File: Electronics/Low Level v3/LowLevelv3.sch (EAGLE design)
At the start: 53 parts, among them IC2 MCP4802, K1 ORWH-SH-105D1F,000, K3 ORWH-SH-105D1F,000, Q1 16MHz, T1 2N3904, T2 2N3904, U1 284512-4, U4 MCP2515, U5 MCP2551DIL08, X1 DB9 Plug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

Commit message: electronics update!
moved a lot of stuff to get the board smaller, added ground planes, added CANbus 3-pin header, fixed all the silkscreening
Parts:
- removed C12: 0.1uF, SparkFun-Capacitors:0.1UF-25V(+80/-20%)(0603)
- removed C14, C15: 22pF, SparkFun-Capacitors:22PF-PTH-2.54MM-200V-5%
- removed ODO_PORT_SELECT: (no value), pinhead:PINHD-1X3
- removed R12, R13: 100, SparkFun-Resistors:100OHM-1/10W-1%(0603)
- removed R14: 4.7K, SparkFun-Resistors:4.7KOHM-1/10W-1%(0603)
- removed U$2: CUI_JACKTHROUGH_HOLE, Elcano:CUI_JACKTHROUGH_HOLE
- added C13, C7: 560pF, rcl:C-US025-025X050
- added J1: (no value), SparkFun-Connectors:CONN_03-SCREW-5MM
- added R10, R7: 100, rcl:R-US_0207/10
- added R11: 4.7K, rcl:R-US_0207/10
- C1: value 560pF -> 0.1uF; device SparkFun-Capacitors:560PF-50V-5%(0603) -> rcl:C-US025-025X050; SPICEPREFIX C -> (none)
- C10: value 1 uF -> 0.1uF; device rcl:C-US025-030X050 -> rcl:C-US025-025X050
- C11: value 560pF -> 22pF; device SparkFun-Capacitors:560PF-50V-5%(0603) -> rcl:C-US025-025X050; SPICEPREFIX C -> (none)
- C6: value 0.1uF -> 22pF; device SparkFun-Capacitors:0.1UF-25V(+80/-20%)(0603) -> rcl:C-US025-025X050; SPICEPREFIX C -> (none)
- renumbered X1 to CANBUS
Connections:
- net SOLENOID_GND renamed SOLENOID_COMMON
- removed net N$1: C10.1, ODO_PORT_SELECT.3, U$2.P$1
- removed net N$15: D2.C, K3.C1
- removed net N$4: C4.1, ODO_PORT_SELECT.1, X4.1
- removed net N$8: D3.C, K1.C1
- new net RX3: CANBUS.8, COMM_DIG.7
- new net TX3: CANBUS.6, COMM_DIG.8
- net 5V: now also C1.1, C10.1, D2.C, D3.C, K1.C1, K3.C1; no longer C12.2, C6.2
- net CANH: now also J1.2, R7.2; no longer R13.2
- net CANL: now also J1.3, R10.2; no longer R12.2
- net GND: now also C1.2, C11.2, C13.2, C6.2, C7.2, CANBUS.1, J1.1, R11.2; no longer C1.1, C11.1, C12.1, C14.1, C15.1, C6.1, R14.1, U$2.P$2, U$2.P$3
- net N$10: now also C13.1, R7.1; no longer C11.2, R13.1
- net N$14: now also R11.1; no longer R14.2
- net N$17: now also C6.1; no longer C15.2
- net N$18: now also C11.1; no longer C14.2
- net N$9: now also C7.1, R10.1; no longer C1.2, R12.1
- net WHEELROTATION: now also C4.1, X4.1; no longer ODO_PORT_SELECT.2
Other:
- moved on the sheet: C1, C10, C11, C6, D1, U1

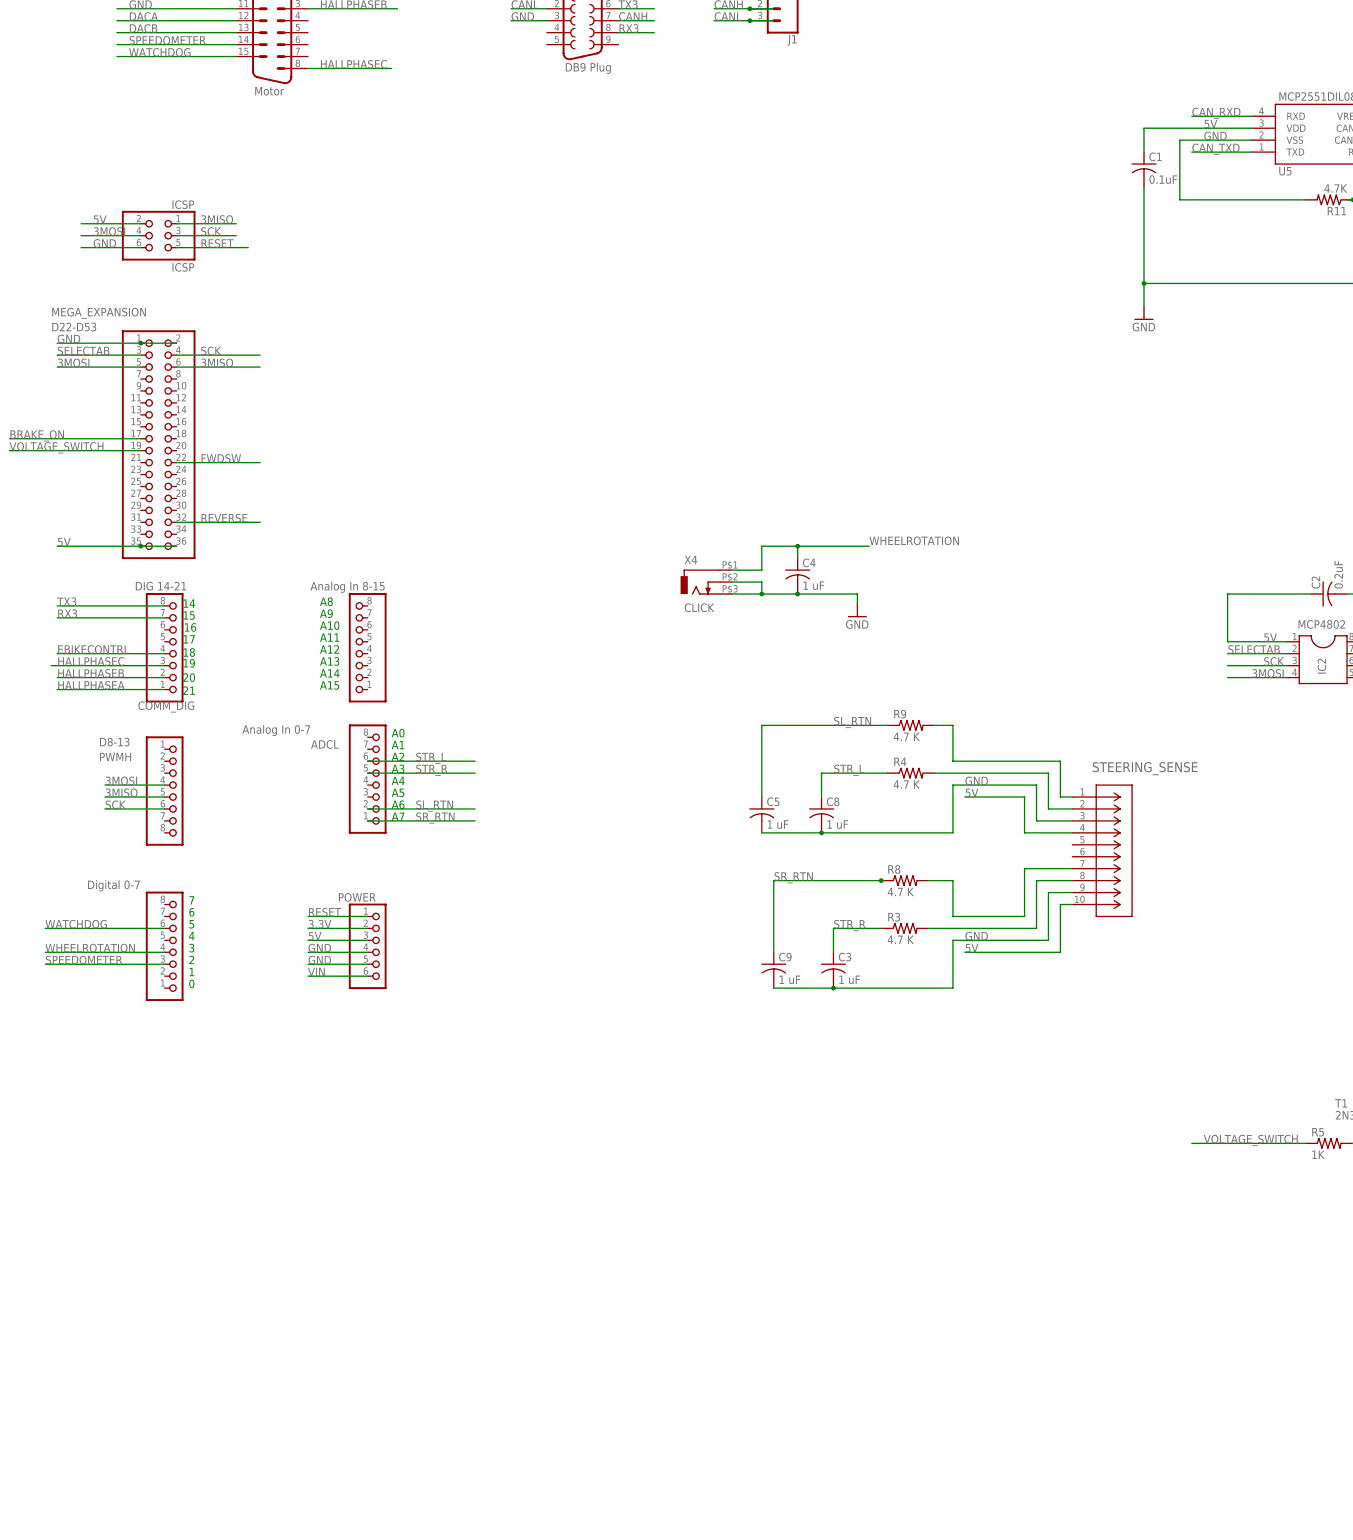
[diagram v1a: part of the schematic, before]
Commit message: added PWM output on steering header and 120ohm terminating resistor for CAN
forgot to commit this...
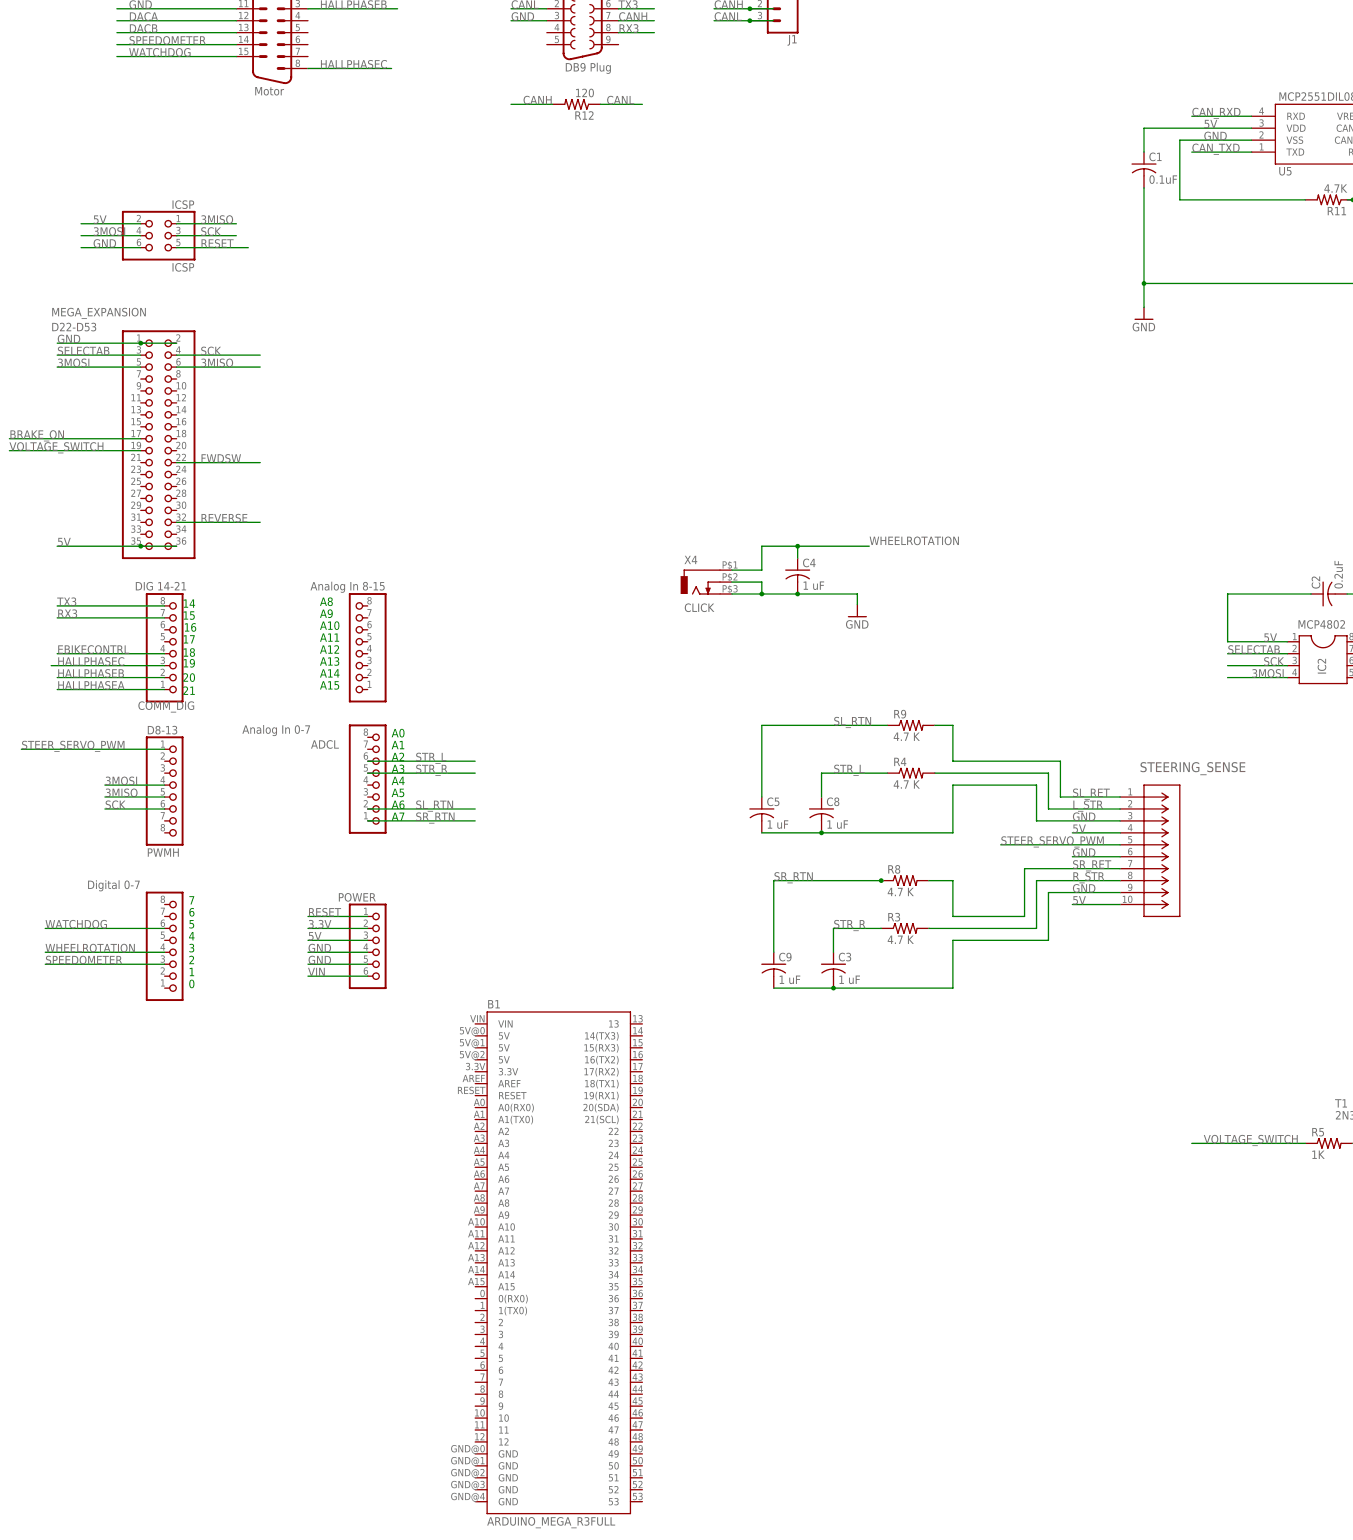
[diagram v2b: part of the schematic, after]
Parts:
- added B1: ARDUINO_MEGA_R3FULL, SparkFun-Boards:ARDUINO_MEGA_R3FULL
- added R12: 120, rcl:R-US_0207/10
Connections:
- new net STEER_SERVO_PWM: D8-13.1, STEERING_SENSE.5
- net CANH: now also R12.2
- net CANL: now also R12.1
- net GND: now also STEERING_SENSE.6
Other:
- moved on the sheet: STEERING_SENSE
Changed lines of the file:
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@@
 <part name="C11" library="rcl" library_urn="urn:adsk.eagle:library:334" deviceset="C-US" device="025-025X050" package3d_urn="urn:adsk.eagle:package:23629/2" value="22pF"/>
 <part name="J1" library="SparkFun-Connectors" library_urn="urn:adsk.eagle:library:513" deviceset="CONN_03" device="-SCREW-5MM" package3d_urn="urn:adsk.eagle:package:38070/1"/>
+<part name="R12" library="rcl" library_urn="urn:adsk.eagle:library:334" deviceset="R-US_" device="0207/10" package3d_urn="urn:adsk.eagle:package:23491/2" value="120"/>
+<part name="B1" library="SparkFun-Boards" library_urn="urn:adsk.eagle:library:509" deviceset="ARDUINO_MEGA_R3" device="FULL" package3d_urn="urn:adsk.eagle:package:37320/1"/>
 </parts>
 <sheets>
@@
 </instance>
 <instance part="D8-13" gate="A" x="58.42" y="55.88" smashed="yes">
-<attribute name="NAME" x="41.91" y="66.675" size="1.778" layer="95"/>
-<attribute name="VALUE" x="41.91" y="63.5" size="1.778" layer="96"/>
+<attribute name="NAME" x="52.07" y="69.215" size="1.778" layer="95"/>
+<attribute name="VALUE" x="52.07" y="43.18" size="1.778" layer="96"/>
 </instance>
 <instance part="GND5" gate="1" x="203.2" y="94.234" smashed="yes">
@@
 <attribute name="VALUE" x="383.52096875" y="-27.711740625" size="1.77906875" layer="96"/>
 </instance>
-<instance part="STEERING_SENSE" gate="A" x="248.92" y="55.88" smashed="yes">
-<attribute name="NAME" x="253.0856" y="61.1886" size="2.0828" layer="95" ratio="6" rot="SR0"/>
+<instance part="STEERING_SENSE" gate="A" x="259.08" y="55.88" smashed="yes">
+<attribute name="NAME" x="263.2456" y="61.1886" size="2.0828" layer="95" ratio="6" rot="SR0"/>
 </instance>
 <instance part="C7" gate="G$1" x="327.66" y="175.26" smashed="yes">
@@
 <attribute name="VALUE" x="190.5" y="230.886" size="1.778" layer="96" font="vector" rot="R180"/>
 <attribute name="NAME" x="190.5" y="217.932" size="1.778" layer="95" font="vector" rot="R180"/>
+</instance>
+<instance part="R12" gate="G$1" x="143.51" y="203.2" smashed="yes" rot="R180">
+<attribute name="NAME" x="147.32" y="201.7014" size="1.778" layer="95" rot="R180"/>
+<attribute name="VALUE" x="147.32" y="206.502" size="1.778" layer="96" rot="R180"/>
+</instance>
+<instance part="B1" gate="G$1" x="139.7" y="-43.18" smashed="yes">
+<attribute name="NAME" x="124.46" y="10.922" size="1.778" layer="95"/>
+<attribute name="VALUE" x="124.46" y="-99.06" size="1.778" layer="96"/>
 </instance>
 </instances>
@@
 </segment>
 <segment>
-<label x="226.06" y="22.86" size="1.778" layer="95"/>
-<wire x1="226.06" y1="22.86" x2="246.38" y2="22.86" width="0.1524" layer="91"/>
-<wire x1="246.38" y1="22.86" x2="246.38" y2="33.02" width="0.1524" layer="91"/>
+<label x="248.92" y="33.02" size="1.778" layer="95"/>
 <pinref part="STEERING_SENSE" gate="A" pin="10"/>
-<wire x1="246.38" y1="33.02" x2="248.92" y2="33.02" width="0.1524" layer="91"/>
+<wire x1="248.92" y1="33.02" x2="259.08" y2="33.02" width="0.1524" layer="91"/>
 </segment>
 <segment>
@@
 </segment>
 <segment>
-<wire x1="238.76" y1="55.88" x2="226.06" y2="55.88" width="0.1524" layer="91"/>
-<label x="226.06" y="55.88" size="1.778" layer="95"/>
-<wire x1="238.76" y1="55.88" x2="238.76" y2="48.26" width="0.1524" layer="91"/>
+<label x="248.92" y="48.26" size="1.778" layer="95"/>
 <pinref part="STEERING_SENSE" gate="A" pin="4"/>
-<wire x1="238.76" y1="48.26" x2="248.92" y2="48.26" width="0.1524" layer="91"/>
+<wire x1="248.92" y1="48.26" x2="259.08" y2="48.26" width="0.1524" layer="91"/>
 </segment>
 <segment>
@@
 <wire x1="223.52" y1="15.24" x2="223.52" y2="25.4" width="0.1524" layer="91"/>
 <wire x1="243.84" y1="25.4" x2="223.52" y2="25.4" width="0.1524" layer="91"/>
-<label x="226.06" y="25.4" size="1.778" layer="95"/>
+<label x="248.92" y="35.56" size="1.778" layer="95"/>
 <wire x1="243.84" y1="25.4" x2="243.84" y2="35.56" width="0.1524" layer="91"/>
 <pinref part="STEERING_SENSE" gate="A" pin="9"/>
-<wire x1="243.84" y1="35.56" x2="248.92" y2="35.56" width="0.1524" layer="91"/>
+<wire x1="243.84" y1="35.56" x2="259.08" y2="35.56" width="0.1524" layer="91"/>
 </segment>
 <segment>
@@
 <wire x1="195.58" y1="48.26" x2="223.52" y2="48.26" width="0.1524" layer="91"/>
 <wire x1="223.52" y1="48.26" x2="223.52" y2="58.42" width="0.1524" layer="91"/>
-<label x="226.06" y="58.42" size="1.778" layer="95"/>
+<label x="248.92" y="50.8" size="1.778" layer="95"/>
 <wire x1="195.58" y1="48.26" x2="182.88" y2="48.26" width="0.1524" layer="91"/>
 <junction x="195.58" y="48.26"/>
 <pinref part="STEERING_SENSE" gate="A" pin="3"/>
 <wire x1="241.3" y1="58.42" x2="241.3" y2="50.8" width="0.1524" layer="91"/>
-<wire x1="241.3" y1="50.8" x2="248.92" y2="50.8" width="0.1524" layer="91"/>
+<wire x1="241.3" y1="50.8" x2="259.08" y2="50.8" width="0.1524" layer="91"/>
 </segment>
 <segment>
@@
 <wire x1="137.16" y1="226.06" x2="129.54" y2="226.06" width="0.1524" layer="91"/>
 <label x="129.54" y="226.06" size="1.778" layer="95"/>
+</segment>
+<segment>
+<pinref part="STEERING_SENSE" gate="A" pin="6"/>
+<wire x1="259.08" y1="43.18" x2="248.92" y2="43.18" width="0.1524" layer="91"/>
+<label x="248.92" y="43.18" size="1.778" layer="95"/>
 </segment>
 </net>
@@
 <wire x1="241.3" y1="27.94" x2="241.3" y2="38.1" width="0.1524" layer="91"/>
 <pinref part="STEERING_SENSE" gate="A" pin="8"/>
-<wire x1="241.3" y1="38.1" x2="248.92" y2="38.1" width="0.1524" layer="91"/>
+<wire x1="241.3" y1="38.1" x2="259.08" y2="38.1" width="0.1524" layer="91"/>
+<label x="248.92" y="38.1" size="1.778" layer="95"/>
 </segment>
 </net>
@@
 <wire x1="243.84" y1="60.96" x2="243.84" y2="53.34" width="0.1524" layer="91"/>
 <pinref part="STEERING_SENSE" gate="A" pin="2"/>
-<wire x1="243.84" y1="53.34" x2="248.92" y2="53.34" width="0.1524" layer="91"/>
+<wire x1="243.84" y1="53.34" x2="259.08" y2="53.34" width="0.1524" layer="91"/>
+<label x="248.92" y="53.34" size="1.778" layer="95"/>
 </segment>
 </net>
@@
 <wire x1="246.38" y1="63.5" x2="246.38" y2="55.88" width="0.1524" layer="91"/>
 <pinref part="STEERING_SENSE" gate="A" pin="1"/>
-<wire x1="246.38" y1="55.88" x2="248.92" y2="55.88" width="0.1524" layer="91"/>
+<wire x1="246.38" y1="55.88" x2="259.08" y2="55.88" width="0.1524" layer="91"/>
+<label x="248.92" y="55.88" size="1.778" layer="95"/>
 </segment>
 </net>
@@
 <wire x1="238.76" y1="30.48" x2="238.76" y2="40.64" width="0.1524" layer="91"/>
 <pinref part="STEERING_SENSE" gate="A" pin="7"/>
-<wire x1="238.76" y1="40.64" x2="248.92" y2="40.64" width="0.1524" layer="91"/>
+<wire x1="238.76" y1="40.64" x2="259.08" y2="40.64" width="0.1524" layer="91"/>
+<label x="248.92" y="40.64" size="1.778" layer="95"/>
 </segment>
 </net>
@@
 <wire x1="180.34" y1="223.52" x2="172.72" y2="223.52" width="0.1524" layer="91"/>
 <junction x="180.34" y="223.52"/>
+</segment>
+<segment>
+<pinref part="R12" gate="G$1" pin="2"/>
+<wire x1="138.43" y1="203.2" x2="129.54" y2="203.2" width="0.1524" layer="91"/>
+<label x="132.08" y="203.2" size="1.778" layer="95"/>
 </segment>
 </net>
@@
 <wire x1="180.34" y1="220.98" x2="172.72" y2="220.98" width="0.1524" layer="91"/>
 <junction x="180.34" y="220.98"/>
+</segment>
+<segment>
+<pinref part="R12" gate="G$1" pin="1"/>
+<wire x1="148.59" y1="203.2" x2="157.48" y2="203.2" width="0.1524" layer="91"/>
+<label x="149.86" y="203.2" size="1.778" layer="95"/>
 </segment>
 </net>
@@
 </segment>
 </net>
+<net name="STEER_SERVO_PWM" class="0">
+<segment>
+<pinref part="D8-13" gate="A" pin="1"/>
+<wire x1="55.88" y1="66.04" x2="25.4" y2="66.04" width="0.1524" layer="91"/>
+<label x="25.4" y="66.04" size="1.778" layer="95"/>
+</segment>
+<segment>
+<pinref part="STEERING_SENSE" gate="A" pin="5"/>
+<wire x1="259.08" y1="45.72" x2="233.68" y2="45.72" width="0.1524" layer="91"/>
+<label x="233.68" y="45.72" size="1.778" layer="95"/>
+</segment>
+</net>
